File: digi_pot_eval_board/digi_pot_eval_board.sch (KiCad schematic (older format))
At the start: 27 parts, among them J1 Conn_01x07_Male, J2 Conn_01x10_Male, K2 G6K2FYTR5DC, K4 G6K2FYTR5DC, K5 G6K2FYTR5DC, K6 G6K2FYTR5DC, K7 G6K2FYTR5DC, SW3 SW_Push, U1 DigiPot, U2 DigiPot, U3 DigiPot, U4 DigiPot, U5 DigiPot, U6 DigiPot, U7 DigiPot, U8 ULN2003A

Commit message: Before wide nav_panel and Level pot move.
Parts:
- added J10, J9: AudioJack3, Connectors:phone-jack-6.3, symbol Connector:AudioJack3
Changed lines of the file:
@@
 EESchema Schematic File Version 4
+LIBS:digi_pot_eval_board-cache
 EELAYER 26 0
 EELAYER END
@@
 Wire Wire Line
 	4300 1800 4300 1900
+$Comp
+L Connector:AudioJack3 J9
+U 1 1 5DA7B145
+P 10250 3600
+F 0 "J9" H 10230 3925 50  0000 C CNN
+F 1 "AudioJack3" H 10230 3834 50  0000 C CNN
+F 2 "Connectors:phone-jack-6.3" H 10250 3600 50  0001 C CNN
+F 3 "~" H 10250 3600 50  0001 C CNN
+	1    10250 3600
+	1    0    0    -1
+$EndComp
+$Comp
+L Connector:AudioJack3 J10
+U 1 1 5DB2E39C
+P 10250 4250
+F 0 "J10" H 10230 4575 50  0000 C CNN
+F 1 "AudioJack3" H 10230 4484 50  0000 C CNN
+F 2 "Connectors:phone-jack-6.3" H 10250 4250 50  0001 C CNN
+F 3 "~" H 10250 4250 50  0001 C CNN
+	1    10250 4250
+	1    0    0    -1
+$EndComp
 $EndSCHEMATC

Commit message: Introducing new layout.
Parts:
- removed J10, J9: AudioJack3, Connectors:phone-jack-6.3, symbol Connector:AudioJack3
- PAN1: footprint nav_panel:nav_panel_THT -> nav_panel:nav_panel_SMD
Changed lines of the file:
@@
 F 0 "PAN1" H 9850 1900 50  0000 C CNN
 F 1 "nav_panel" H 10350 1900 50  0000 C CNN
-F 2 "nav_panel:nav_panel_THT" H 10100 1650 50  0001 C CNN
+F 2 "nav_panel:nav_panel_SMD" H 10100 1650 50  0001 C CNN
 F 3 "" H 10100 1650 50  0001 C CNN
 	1    10100 1550
@@
 Wire Wire Line
 	4300 1800 4300 1900
-$Comp
-L Connector:AudioJack3 J9
-U 1 1 5DA7B145
-P 10250 3600
-F 0 "J9" H 10230 3925 50  0000 C CNN
-F 1 "AudioJack3" H 10230 3834 50  0000 C CNN
-F 2 "Connectors:phone-jack-6.3" H 10250 3600 50  0001 C CNN
-F 3 "~" H 10250 3600 50  0001 C CNN
-	1    10250 3600
-	1    0    0    -1
-$EndComp
-$Comp
-L Connector:AudioJack3 J10
-U 1 1 5DB2E39C
-P 10250 4250
-F 0 "J10" H 10230 4575 50  0000 C CNN
-F 1 "AudioJack3" H 10230 4484 50  0000 C CNN
-F 2 "Connectors:phone-jack-6.3" H 10250 4250 50  0001 C CNN
-F 3 "~" H 10250 4250 50  0001 C CNN
-	1    10250 4250
-	1    0    0    -1
-$EndComp
 $EndSCHEMATC

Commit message: Printed and tested layout version.
USB still on upper board.
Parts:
- removed K7: G6K2FYTR5DC, Relay_SMD:Relay_DPDT_Omron_G6K-2F-Y, symbol relay_omron_g6k-2:G6K-2
- removed R6: 10k, Resistor_SMD:R_0805_2012Metric_Pad1.15x1.40mm_HandSolder, symbol Device:R
- removed SW3: SW_Push, Button_Switch_SMD:SW_SPST_B3S-1000, symbol Switch:SW_Push
- added J4: Conn_01x02_Male, Connector_JST:JST_EH_B02B-EH-A_1x02_P2.50mm_Vertical, symbol Connector:Conn_01x02_Male
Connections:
- net labels removed: SW_PASSBACK
- wire segments 87 -> 83
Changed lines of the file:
@@
 PW1
-$Comp
-L relay_omron_g6k-2:G6K-2 K7
-U 1 1 5D8C5BA8
-P 5850 5750
-F 0 "K7" H 6480 5796 50  0000 L CNN
-F 1 "G6K2FYTR5DC" H 6480 5705 50  0000 L CNN
-F 2 "Relay_SMD:Relay_DPDT_Omron_G6K-2F-Y" H 6300 5650 50  0001 C CNN
-F 3 "http://cdn-reichelt.de/documents/datenblatt/C300/G6H%23OMR.pdf" H 6500 5900 50  0001 C CNN
-F 4 "BYPASS" H 5850 5750 50  0001 C CNN "Label"
-	1    5850 5750
-	0    -1   1    0
-$EndComp
 $Comp
 L Transistor_Array:ULN2003A U8
@@
 L power:+5V #PWR0126
 U 1 1 5D8CDA36
-P 5500 5300
-F 0 "#PWR0126" H 5500 5150 50  0001 C CNN
-F 1 "+5V" H 5515 5473 50  0000 C CNN
-F 2 "" H 5500 5300 50  0001 C CNN
-F 3 "" H 5500 5300 50  0001 C CNN
-	1    5500 5300
+P 7000 5600
+F 0 "#PWR0126" H 7000 5450 50  0001 C CNN
+F 1 "+5V" H 7015 5773 50  0000 C CNN
+F 2 "" H 7000 5600 50  0001 C CNN
+F 3 "" H 7000 5600 50  0001 C CNN
+	1    7000 5600
 	1    0    0    -1
 $EndComp
@@
 Text GLabel 5100 5300 1    50   Input ~ 0
 KLW_SINK
-Wire Wire Line
-	5500 5300 5500 5350
-Wire Wire Line
-	5500 5350 5550 5350
-Text GLabel 6200 5300 1    50   Input ~ 0
+Text GLabel 6950 5750 2    50   Input ~ 0
 KBP_SINK
 Text GLabel 8950 5600 2    50   Input ~ 0
@@
 Text GLabel 8950 5200 2    50   Input ~ 0
 KBP_SINK
-$Comp
-L Switch:SW_Push SW3
-U 1 1 5D8D0066
-P 10250 2450
-F 0 "SW3" H 10250 2735 50  0000 C CNN
-F 1 "SW_Push" H 10250 2644 50  0000 C CNN
-F 2 "Button_Switch_SMD:SW_SPST_B3S-1000" H 10250 2650 50  0001 C CNN
-F 3 "" H 10250 2650 50  0001 C CNN
-	1    10250 2450
-	1    0    0    -1
-$EndComp
-$Comp
-L power:+5V #PWR0131
-U 1 1 5D8D006C
-P 10500 2350
-F 0 "#PWR0131" H 10500 2200 50  0001 C CNN
-F 1 "+5V" H 10515 2523 50  0000 C CNN
-F 2 "" H 10500 2350 50  0001 C CNN
-F 3 "" H 10500 2350 50  0001 C CNN
-	1    10500 2350
-	1    0    0    -1
-$EndComp
-$Comp
-L Device:R R6
-U 1 1 5D8D0072
-P 10050 2600
-F 0 "R6" H 10120 2646 50  0000 L CNN
-F 1 "10k" V 10050 2600 39  0000 C CNN
-F 2 "Resistor_SMD:R_0805_2012Metric_Pad1.15x1.40mm_HandSolder" V 9980 2600 50  0001 C CNN
-F 3 "~" H 10050 2600 50  0001 C CNN
-	1    10050 2600
-	1    0    0    -1
-$EndComp
-$Comp
-L power:GND #PWR0132
-U 1 1 5D8D0078
-P 10050 2750
-F 0 "#PWR0132" H 10050 2500 50  0001 C CNN
-F 1 "GND" H 9900 2650 50  0000 C CNN
-F 2 "" H 10050 2750 50  0001 C CNN
-F 3 "" H 10050 2750 50  0001 C CNN
-	1    10050 2750
-	1    0    0    -1
-$EndComp
-Wire Wire Line
-	10450 2450 10500 2450
-Wire Wire Line
-	10500 2450 10500 2350
 $Comp
 L Connector:Conn_01x10_Male J2
@@
 Text GLabel 10600 1500 2    50   Input ~ 0
 SW_RIGHT
-Text GLabel 9950 2450 0    50   Input ~ 0
-SW_PASSBACK
-Wire Wire Line
-	9950 2450 10050 2450
-Connection ~ 10050 2450
 Text GLabel 10600 1650 2    50   Input ~ 0
 SW_STORE
@@
 Wire Wire Line
 	4100 5350 4100 5300
-Wire Wire Line
-	6150 5350 6200 5350
-Wire Wire Line
-	6200 5350 6200 5300
 Text GLabel 1650 2250 0    50   Input ~ 0
 CHG
@@
 Wire Wire Line
 	4300 1800 4300 1900
+$Comp
+L Connector:Conn_01x02_Male J4
+U 1 1 5DCB7D5F
+P 6450 5650
+F 0 "J4" H 6556 5828 50  0000 C CNN
+F 1 "Conn_01x02_Male" H 6556 5737 50  0000 C CNN
+F 2 "Connector_JST:JST_EH_B02B-EH-A_1x02_P2.50mm_Vertical" H 6450 5650 50  0001 C CNN
+F 3 "~" H 6450 5650 50  0001 C CNN
+	1    6450 5650
+	1    0    0    -1
+$EndComp
+Wire Wire Line
+	6650 5650 7000 5650
+Wire Wire Line
+	7000 5650 7000 5600
+Wire Wire Line
+	6650 5750 6950 5750
 $EndSCHEMATC

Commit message: Production version 2019.11.19.
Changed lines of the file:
@@
 L Connector:Conn_01x02_Male J4
 U 1 1 5DCB7D5F
-P 6450 5650
-F 0 "J4" H 6556 5828 50  0000 C CNN
-F 1 "Conn_01x02_Male" H 6556 5737 50  0000 C CNN
-F 2 "Connector_JST:JST_EH_B02B-EH-A_1x02_P2.50mm_Vertical" H 6450 5650 50  0001 C CNN
-F 3 "~" H 6450 5650 50  0001 C CNN
-	1    6450 5650
-	1    0    0    -1
+P 6450 5750
+F 0 "J4" H 6556 5928 50  0000 C CNN
+F 1 "Conn_01x02_Male" H 6556 5837 50  0000 C CNN
+F 2 "Connector_JST:JST_EH_B02B-EH-A_1x02_P2.50mm_Vertical" H 6450 5750 50  0001 C CNN
+F 3 "~" H 6450 5750 50  0001 C CNN
+	1    6450 5750
+	1    0    0    1
 $EndComp
 Wire Wire Line

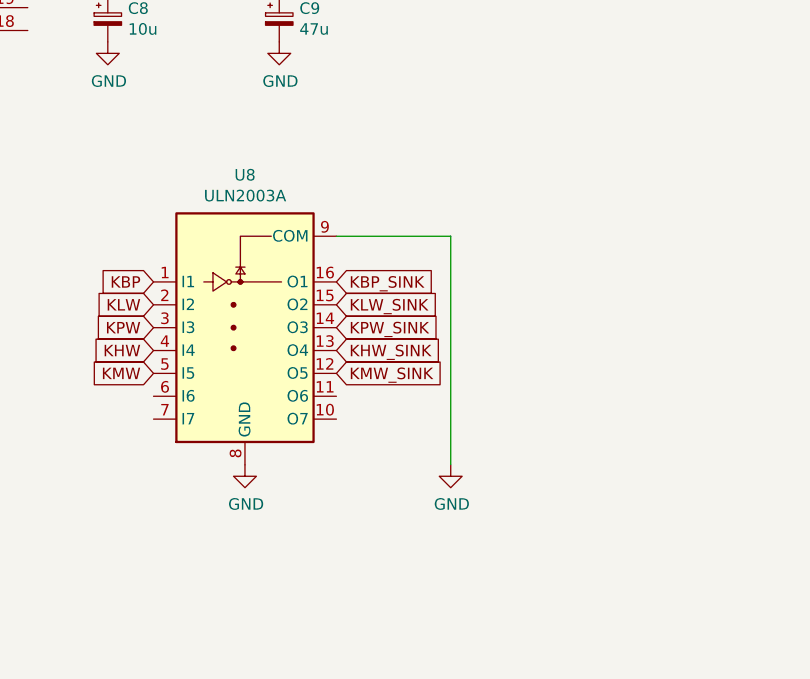
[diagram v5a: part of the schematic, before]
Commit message: Upgrading KiCad and fixing ULN2003a connection.
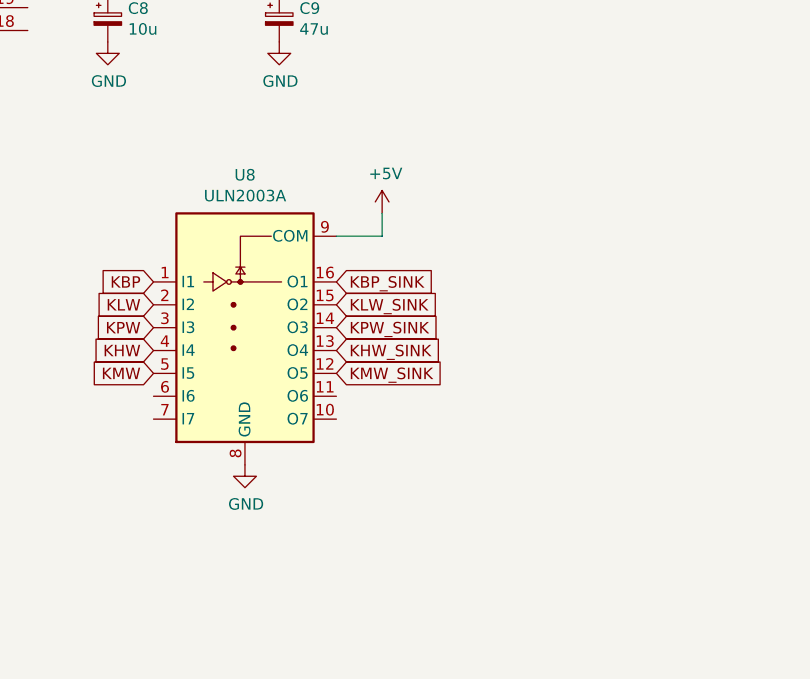
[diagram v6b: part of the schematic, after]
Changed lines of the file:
@@
 EESchema Schematic File Version 4
-LIBS:digi_pot_eval_board-cache
-EELAYER 26 0
+EELAYER 30 0
 EELAYER END
 $Descr A4 11693 8268
@@
 	1    0    0    -1
 $EndComp
-$Comp
-L power:GND #PWR0125
-U 1 1 5D8CD6D8
-P 9450 6000
-F 0 "#PWR0125" H 9450 5750 50  0001 C CNN
-F 1 "GND" H 9455 5827 50  0000 C CNN
-F 2 "" H 9450 6000 50  0001 C CNN
-F 3 "" H 9450 6000 50  0001 C CNN
-	1    9450 6000
-	1    0    0    -1
-$EndComp
-Wire Wire Line
-	8950 5000 9450 5000
 $Comp
 L power:+5V #PWR0126
@@
 Wire Wire Line
 	6250 4000 6250 4600
-Wire Wire Line
-	9450 6000 9450 5000
 $Comp
 L Device:R R25
@@
 Wire Wire Line
 	6650 5750 6950 5750
+$Comp
+L power:+5V #PWR?
+U 1 1 5E2190E4
+P 9150 4900
+F 0 "#PWR?" H 9150 4750 50  0001 C CNN
+F 1 "+5V" H 9165 5073 50  0000 C CNN
+F 2 "" H 9150 4900 50  0001 C CNN
+F 3 "" H 9150 4900 50  0001 C CNN
+	1    9150 4900
+	1    0    0    -1
+$EndComp
+Wire Wire Line
+	8950 5000 9150 5000
+Wire Wire Line
+	9150 5000 9150 4900
 $EndSCHEMATC
